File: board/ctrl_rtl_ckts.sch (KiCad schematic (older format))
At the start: 58 parts, among them J1 Conn_01x04, J2 Conn_01x04, J3 Conn_01x02, Q17 MMBT2369, Q18 MMBT2369, Q19 MMBT2369, Q20 MMBT2369, Q21 MMBT2369, Q22 MMBT2369, Q23 MMBT2369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

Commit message: Board: 5/8 of the data lanes routed
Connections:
- net MSTBSTP renamed MSBSTP
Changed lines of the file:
@@
 $EndComp
 Text GLabel 1050 2950 0    50   Input ~ 0
-MSTBSTP
+MSBSTP
 Wire Wire Line
 	1050 2950 1100 2950

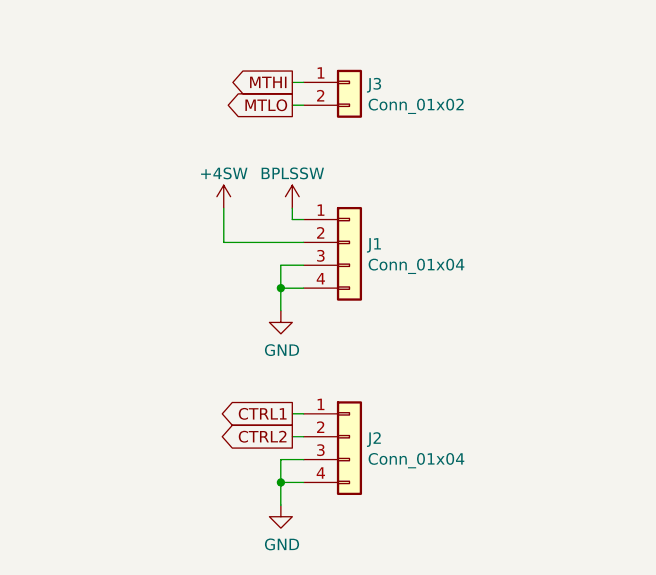
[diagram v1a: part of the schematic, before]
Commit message: Board: Basic layout done, but need to make the board longer to avoid mechanical conflict with the monitor
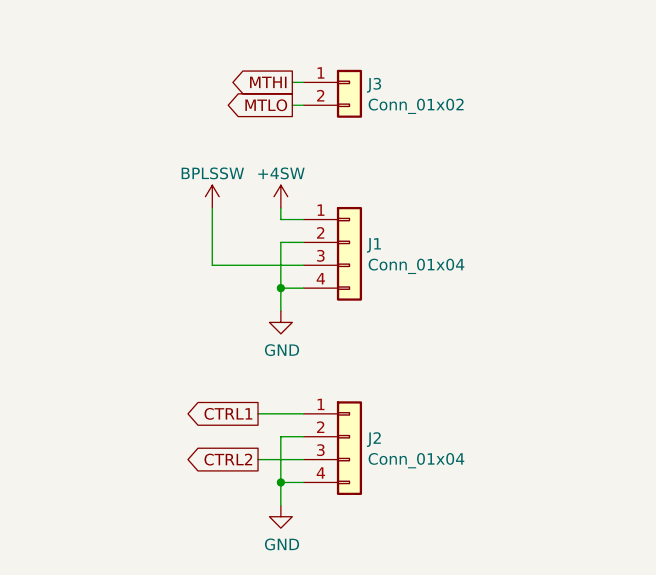
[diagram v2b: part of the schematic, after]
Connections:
- net +4SW: now also J1.1 (Pin_1); no longer J1.2 (Pin_2)
- net BPLSSW: now also J1.3 (Pin_3); no longer J1.1 (Pin_1)
- net CTRL2: now also J2.3 (Pin_3); no longer J2.2 (Pin_2)
- net GND: now also J1.2 (Pin_2), J2.2 (Pin_2); no longer J1.3 (Pin_3), J2.3 (Pin_3)
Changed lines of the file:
@@
 Connection ~ 1750 6250
 Wire Wire Line
-	1750 6150 1750 6250
-Wire Wire Line
-	1850 6150 1750 6150
-Wire Wire Line
-	1500 6050 1850 6050
-Wire Wire Line
-	1500 5900 1500 6050
+	1750 5950 1850 5950
+Wire Wire Line
+	1750 5900 1750 5950
 $Comp
 L agc_monitor:+4SW #PWR?
 U 1 1 5CAD7D18
-P 1500 5900
+P 1750 5900
 AR Path="/5C9CEEB8/5CAD7D18" Ref="#PWR?"  Part="1"
 AR Path="/5CA12007/5CAD7D18" Ref="#PWR?"  Part="1"
 AR Path="/5CA99762/5CAD7D18" Ref="#PWR0105"  Part="1"
-F 0 "#PWR0105" H 1500 5750 50  0001 C CNN
-F 1 "+4SW" H 1500 6050 50  0000 C CNN
-F 2 "" H 1500 5900 50  0001 C CNN
-F 3 "" H 1500 5900 50  0001 C CNN
-	1    1500 5900
-	1    0    0    -1
-$EndComp
-Wire Wire Line
-	1800 5950 1850 5950
-Wire Wire Line
-	1800 5900 1800 5950
+F 0 "#PWR0105" H 1750 5750 50  0001 C CNN
+F 1 "+4SW" H 1750 6050 50  0000 C CNN
+F 2 "" H 1750 5900 50  0001 C CNN
+F 3 "" H 1750 5900 50  0001 C CNN
+	1    1750 5900
+	1    0    0    -1
+$EndComp
 $Comp
 L agc_monitor:BPLSSW #PWR?
 U 1 1 5CAD7D20
-P 1800 5900
+P 1450 5900
 AR Path="/5C9CEEB8/5CAD7D20" Ref="#PWR?"  Part="1"
 AR Path="/5CA12007/5CAD7D20" Ref="#PWR?"  Part="1"
 AR Path="/5CA99762/5CAD7D20" Ref="#PWR0106"  Part="1"
-F 0 "#PWR0106" H 1800 5750 50  0001 C CNN
-F 1 "BPLSSW" H 1800 6050 50  0000 C CNN
-F 2 "" H 1800 5900 50  0001 C CNN
-F 3 "" H 1800 5900 50  0001 C CNN
-	1    1800 5900
+F 0 "#PWR0106" H 1450 5750 50  0001 C CNN
+F 1 "BPLSSW" H 1450 6050 50  0000 C CNN
+F 2 "" H 1450 5900 50  0001 C CNN
+F 3 "" H 1450 5900 50  0001 C CNN
+	1    1450 5900
 	1    0    0    -1
 $EndComp
@@
 	1    0    0    -1
 $EndComp
-Text GLabel 1800 6800 0    50   Output ~ 0
+Text GLabel 1650 6800 0    50   Output ~ 0
 CTRL1
 Wire Wire Line
-	1800 6800 1850 6800
-Wire Wire Line
-	1850 6900 1800 6900
-Text GLabel 1800 6900 0    50   Output ~ 0
+	1650 6800 1850 6800
+Wire Wire Line
+	1850 7000 1650 7000
+Text GLabel 1650 7000 0    50   Output ~ 0
 CTRL2
 $Comp
@@
 	1850 7100 1750 7100
 Connection ~ 1750 7100
-Wire Wire Line
-	1750 7000 1750 7100
-Wire Wire Line
-	1850 7000 1750 7000
 $Comp
 L Device:R_US R?
@@
 Wire Wire Line
 	5250 6800 5250 6750
+Wire Wire Line
+	1750 6050 1850 6050
+Wire Wire Line
+	1750 6050 1750 6250
+Wire Wire Line
+	1450 6150 1850 6150
+Wire Wire Line
+	1450 5900 1450 6150
+Wire Wire Line
+	1750 6900 1850 6900
+Wire Wire Line
+	1750 6900 1750 7100
 $EndSCHEMATC
